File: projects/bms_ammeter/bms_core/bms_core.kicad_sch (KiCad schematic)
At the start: 25 parts, among them J1 CONN_02x03, J2 CONN_02x03, Q1 SSM3K333R, U1 ATMEGA64M1, U2 MAX33011EASA, Y1 Crystal_16MHz_18pF

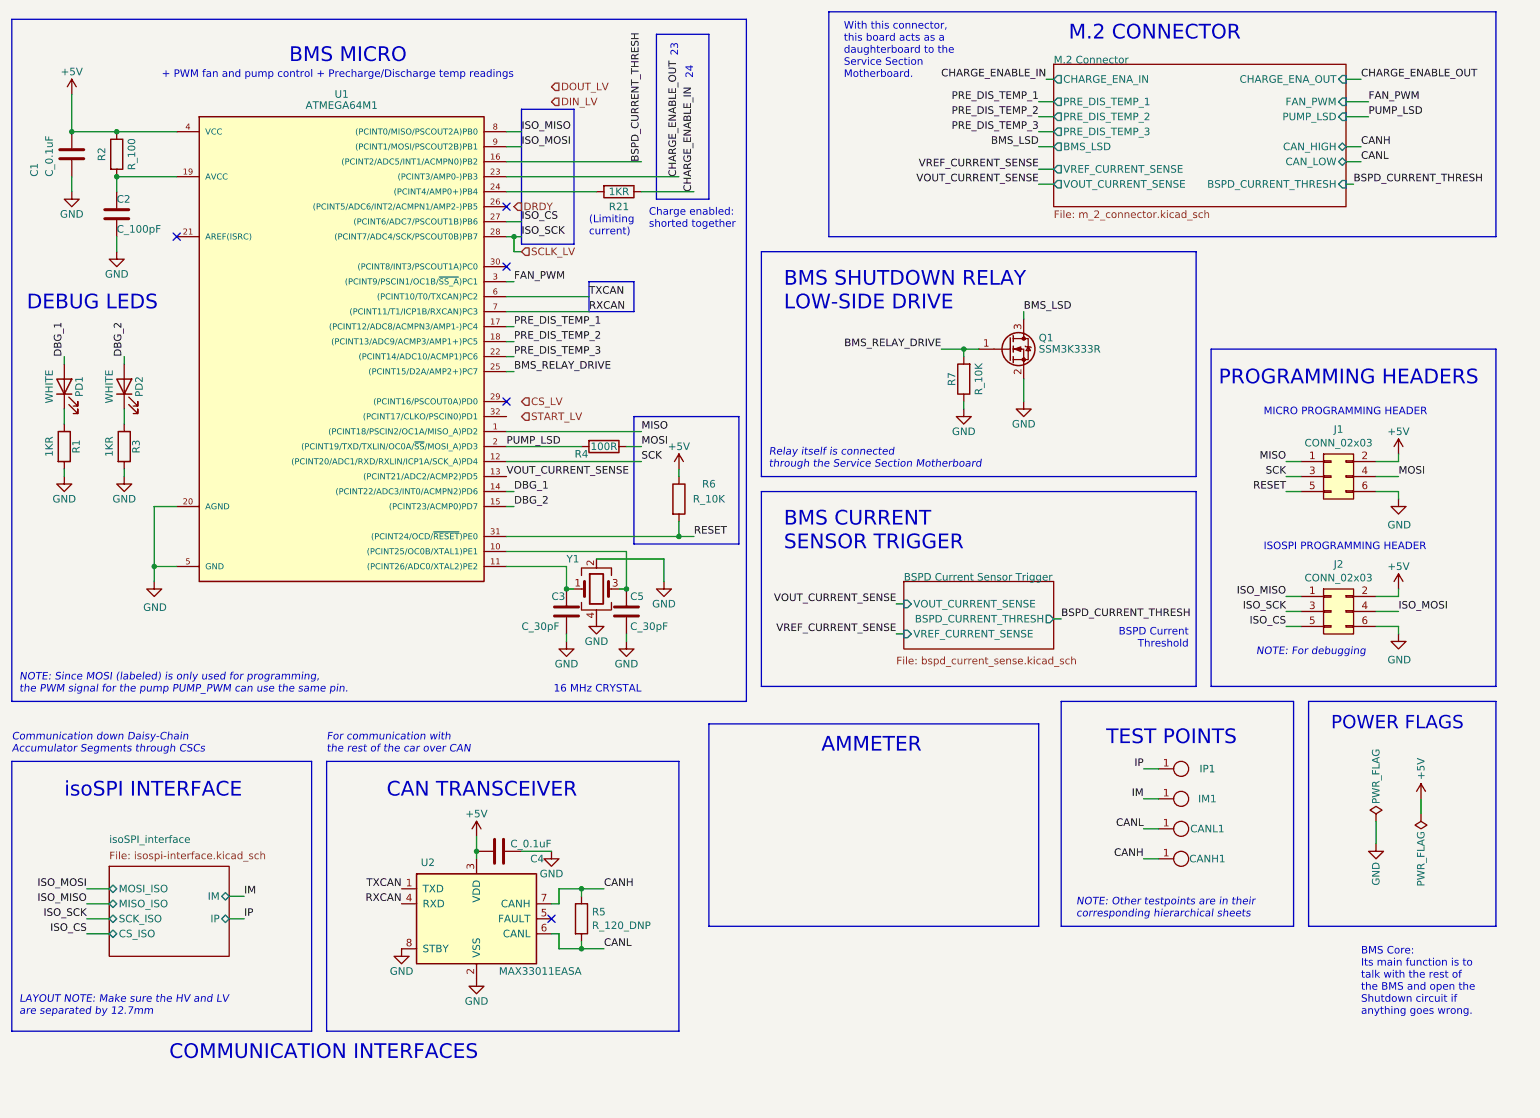
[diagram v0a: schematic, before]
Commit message: Added ammeter to BMS core schematic
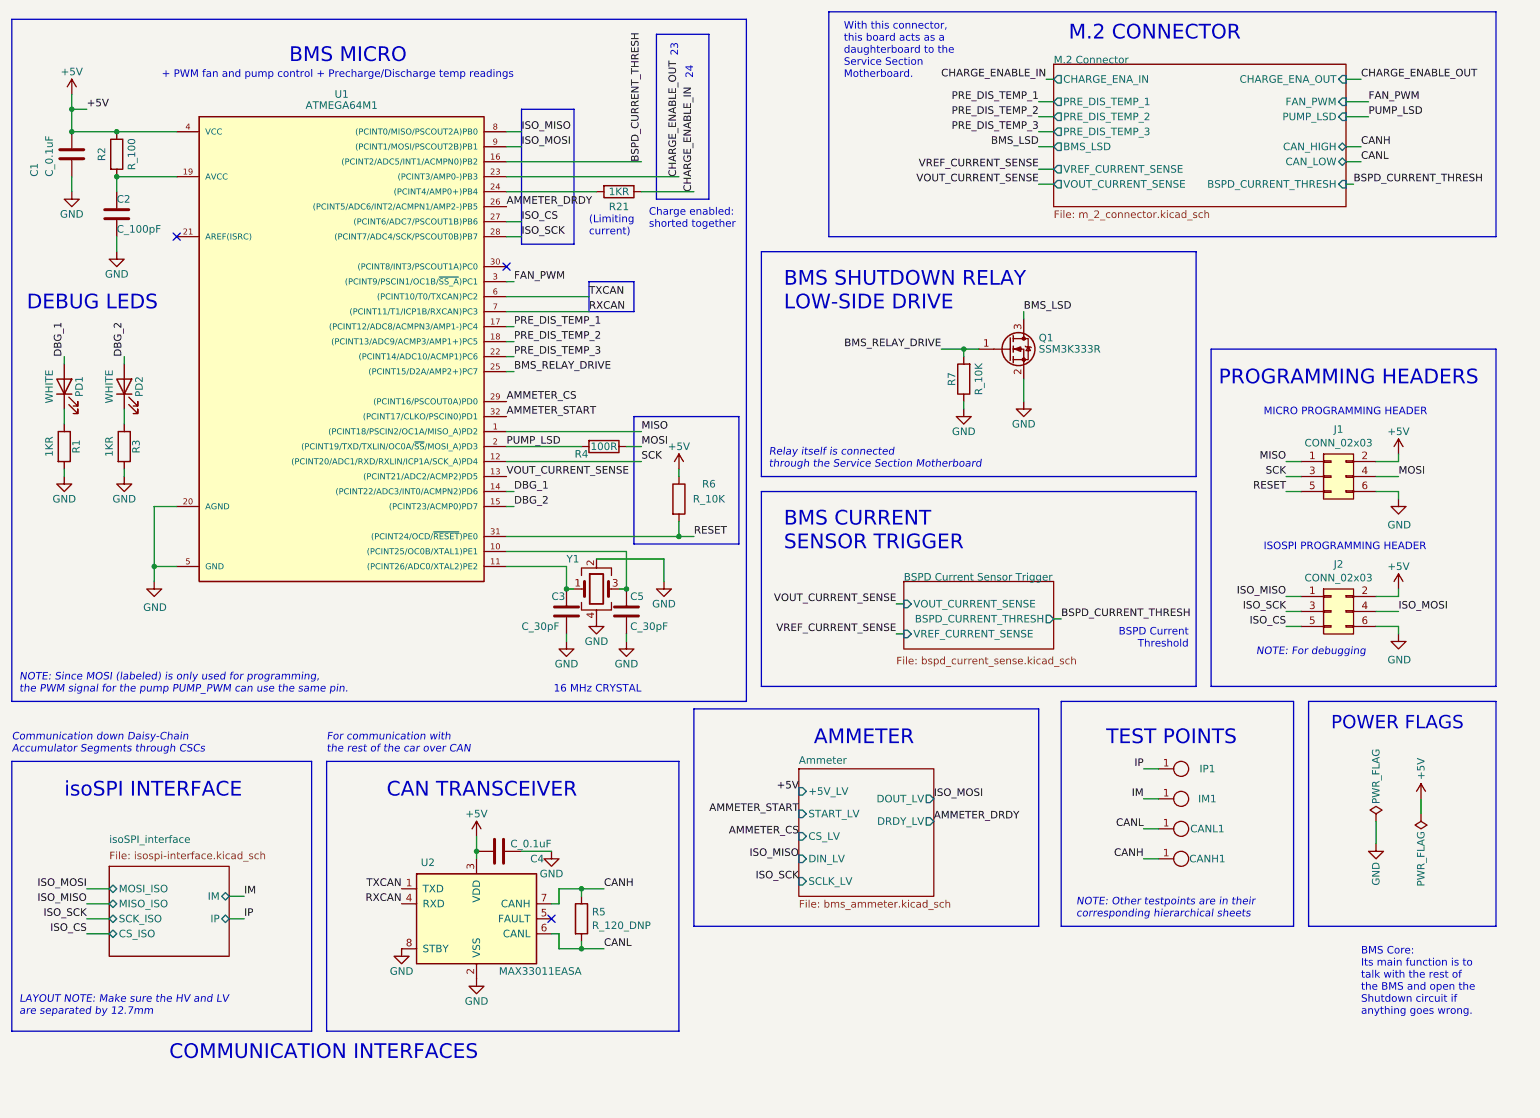
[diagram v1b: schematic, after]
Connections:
- net AMMETER_DRDY: now reaches U1.26 ((PCINT5/ADC6/INT2/ACMPN1/AMP2-)PB5)
- net AMMETER_CS: now reaches U1.29 ((PCINT16/PSCOUT0A)PD0)
- net AMMETER_START: now reaches U1.32 ((PCINT17/CLKO/PSCIN0)PD1)
- net SCLK_LV renamed ISO_SCK
- no-connect marks 5 -> 3
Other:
- added sheet Ammeter (bms_ammeter.kicad_sch)

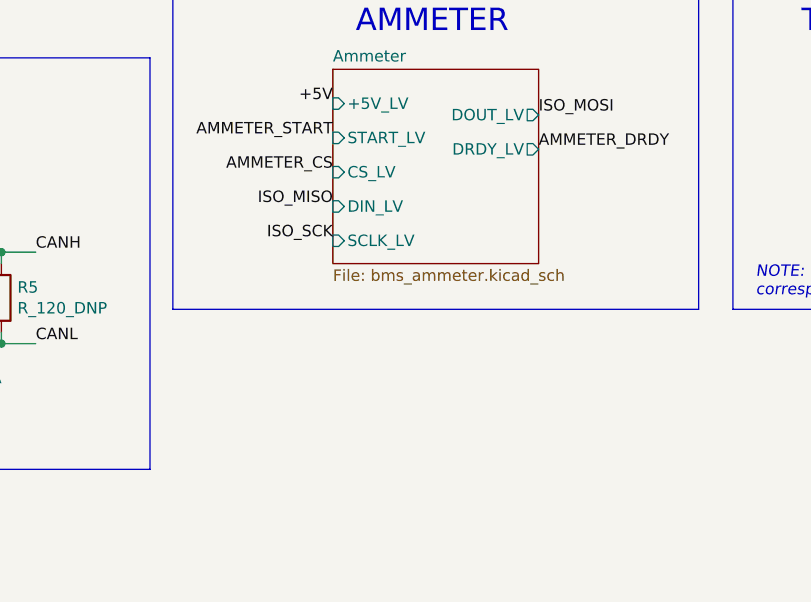
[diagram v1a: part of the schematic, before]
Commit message: Added revisions from Melissa's comments
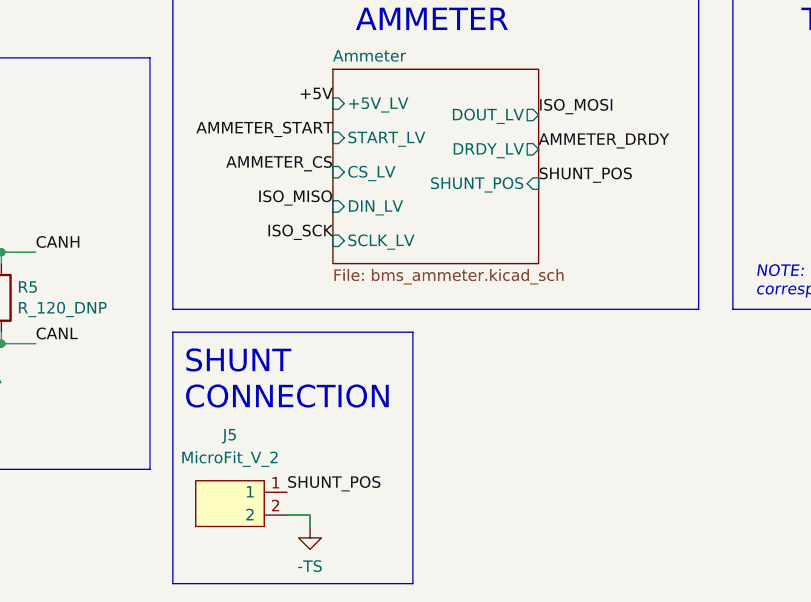
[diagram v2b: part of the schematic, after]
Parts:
- added J5: MicroFit_V_2, footprints:MicroFit_V_2, symbol formula:MicroFit_V_2
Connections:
- new net -TS: J5.2
- new net SHUNT_POS: J5.1
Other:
- sheet Ammeter ports: added SHUNT_POS; removed none
- note added: "SHUNT CONNECTION"
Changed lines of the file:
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@@
+    (stroke (width 0) (type default))
+  )
+  (wire (pts (xy 144.78 194.31) (xy 144.78 193.04))
     (stroke (width 0) (type default))
   )
@@
     (stroke (width 0) (type default))
   )
+  (wire (pts (xy 144.78 193.04) (xy 142.24 193.04))
+    (stroke (width 0) (type default))
+  )
   (wire (pts (xy 175.26 72.39) (xy 177.8 72.39))
     (stroke (width 0) (type default))
@@
   (polyline (pts (xy 111.76 66.04) (xy 119.38 66.04))
     (stroke (width 0) (type default))
+  )
+  (rectangle (start 129.54 172.72) (end 156.21 200.66)
+    (stroke (width 0) (type default))
+    (fill (type none))
   )
   (rectangle (start 129.54 133.35) (end 187.96 170.18)
@@
     (effects (font (size 2.4892 2.4892)) (justify left bottom))
   )
+  (text "SHUNT\nCONNECTION\n" (at 130.81 181.61 0)
+    (effects (font (size 2.4892 2.4892)) (justify left bottom))
+  )
   (text "DEBUG LEDS" (at 16.51 66.04 0)
     (effects (font (size 2.4892 2.4892)) (justify left bottom))
@@
     (effects (font (size 1.27 1.27)) (justify left bottom))
   )
+  (label "SHUNT_POS" (at 142.24 190.5 0) (fields_autoplaced)
+    (effects (font (size 1.27 1.27)) (justify left bottom))
+  )
   (label "MISO" (at 229.87 91.44 180) (fields_autoplaced)
     (effects (font (size 1.27 1.27)) (justify right bottom))
@@
   (label "+5V" (at 147.32 147.32 180) (fields_autoplaced)
     (effects (font (size 1.27 1.27)) (justify right bottom))
+  )
+  (label "SHUNT_POS" (at 170.18 156.21 0) (fields_autoplaced)
+    (effects (font (size 1.27 1.27)) (justify left bottom))
   )
   (label "VREF_CURRENT_SENSE" (at 187.96 41.91 180) (fields_autoplaced)
@@
         (path "/19b2a9f9-0be6-4bde-80c5-cbc5126d55d5"
           (reference "R6") (unit 1)
+        )
+      )
+    )
+  )
+  (symbol (lib_name "-TS_5") (lib_id "formula:-TS") (at 144.78 194.31 0) (unit 1)
+    (in_bom yes) (on_board yes) (dnp no) (fields_autoplaced)
+    (property "Reference" "#PWR013" (at 144.78 200.66 0)
+      (effects (font (size 1.27 1.27)) hide)
+    )
+    (property "Value" "-TS" (at 144.78 198.755 0)
+      (effects (font (size 1.27 1.27)))
+    )
+    (property "Footprint" "" (at 144.78 194.31 0)
+      (effects (font (size 1.27 1.27)) hide)
+    )
+    (property "Datasheet" "" (at 144.78 194.31 0)
+      (effects (font (size 1.27 1.27)) hide)
+    )
+    (pin "1")
+    (instances
+      (project "bms_core"
+        (path "/19b2a9f9-0be6-4bde-80c5-cbc5126d55d5"
+          (reference "#PWR013") (unit 1)
         )
       )
@@
         (path "/19b2a9f9-0be6-4bde-80c5-cbc5126d55d5"
           (reference "#PWR0103") (unit 1)
+        )
+      )
+    )
+  )
+  (symbol (lib_id "formula:MicroFit_V_2") (at 135.89 191.77 0) (unit 1)
+    (in_bom yes) (on_board yes) (dnp no) (fields_autoplaced)
+    (property "Reference" "J5" (at 135.89 184.15 0)
+      (effects (font (size 1.27 1.27)))
+    )
+    (property "Value" "MicroFit_V_2" (at 135.89 186.69 0)
+      (effects (font (size 1.27 1.27)))
+    )
+    (property "Footprint" "footprints:MicroFit_V_2" (at 134.62 186.69 0)
+      (effects (font (size 1.27 1.27)) hide)
+    )
+    (property "Datasheet" "https://www.molex.com/pdm_docs/sd/430450225_sd.pdf" (at 134.62 186.69 0)
+      (effects (font (size 1.27 1.27)) hide)
+    )
+    (property "DK" "MFN" (at 138.43 185.42 0)
+      (effects (font (size 1.27 1.27)) hide)
+    )
+    (property "MPN" "WM10660-ND" (at 140.97 182.88 0)
+      (effects (font (size 1.27 1.27)) hide)
+    )
+    (property "PurchasingLink" "https://www.digikey.com/product-detail/en/molex/0430450225/WM10660-ND/3310180" (at 135.89 187.96 0)
+      (effects (font (size 1.27 1.27)) hide)
+    )
+    (pin "1")
+    (pin "2")
+    (instances
+      (project "bms_core"
+        (path "/19b2a9f9-0be6-4bde-80c5-cbc5126d55d5"
+          (reference "J5") (unit 1)
         )
       )
@@
       (effects (font (size 1.27 1.27)) (justify left))
     )
-    (instances
+    (pin "SHUNT_POS" input (at 170.18 156.21 0)
+      (effects (font (size 1.27 1.27)) (justify right))
+    )
+    (instances
